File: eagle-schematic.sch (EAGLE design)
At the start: 30 parts, among them IC1 74HC595N, IC2 74HC595N, IC3 74HC595N, IC4 74HC595N, J1 DCJ0202, M1 DC-DC_5-15V_TO_5V

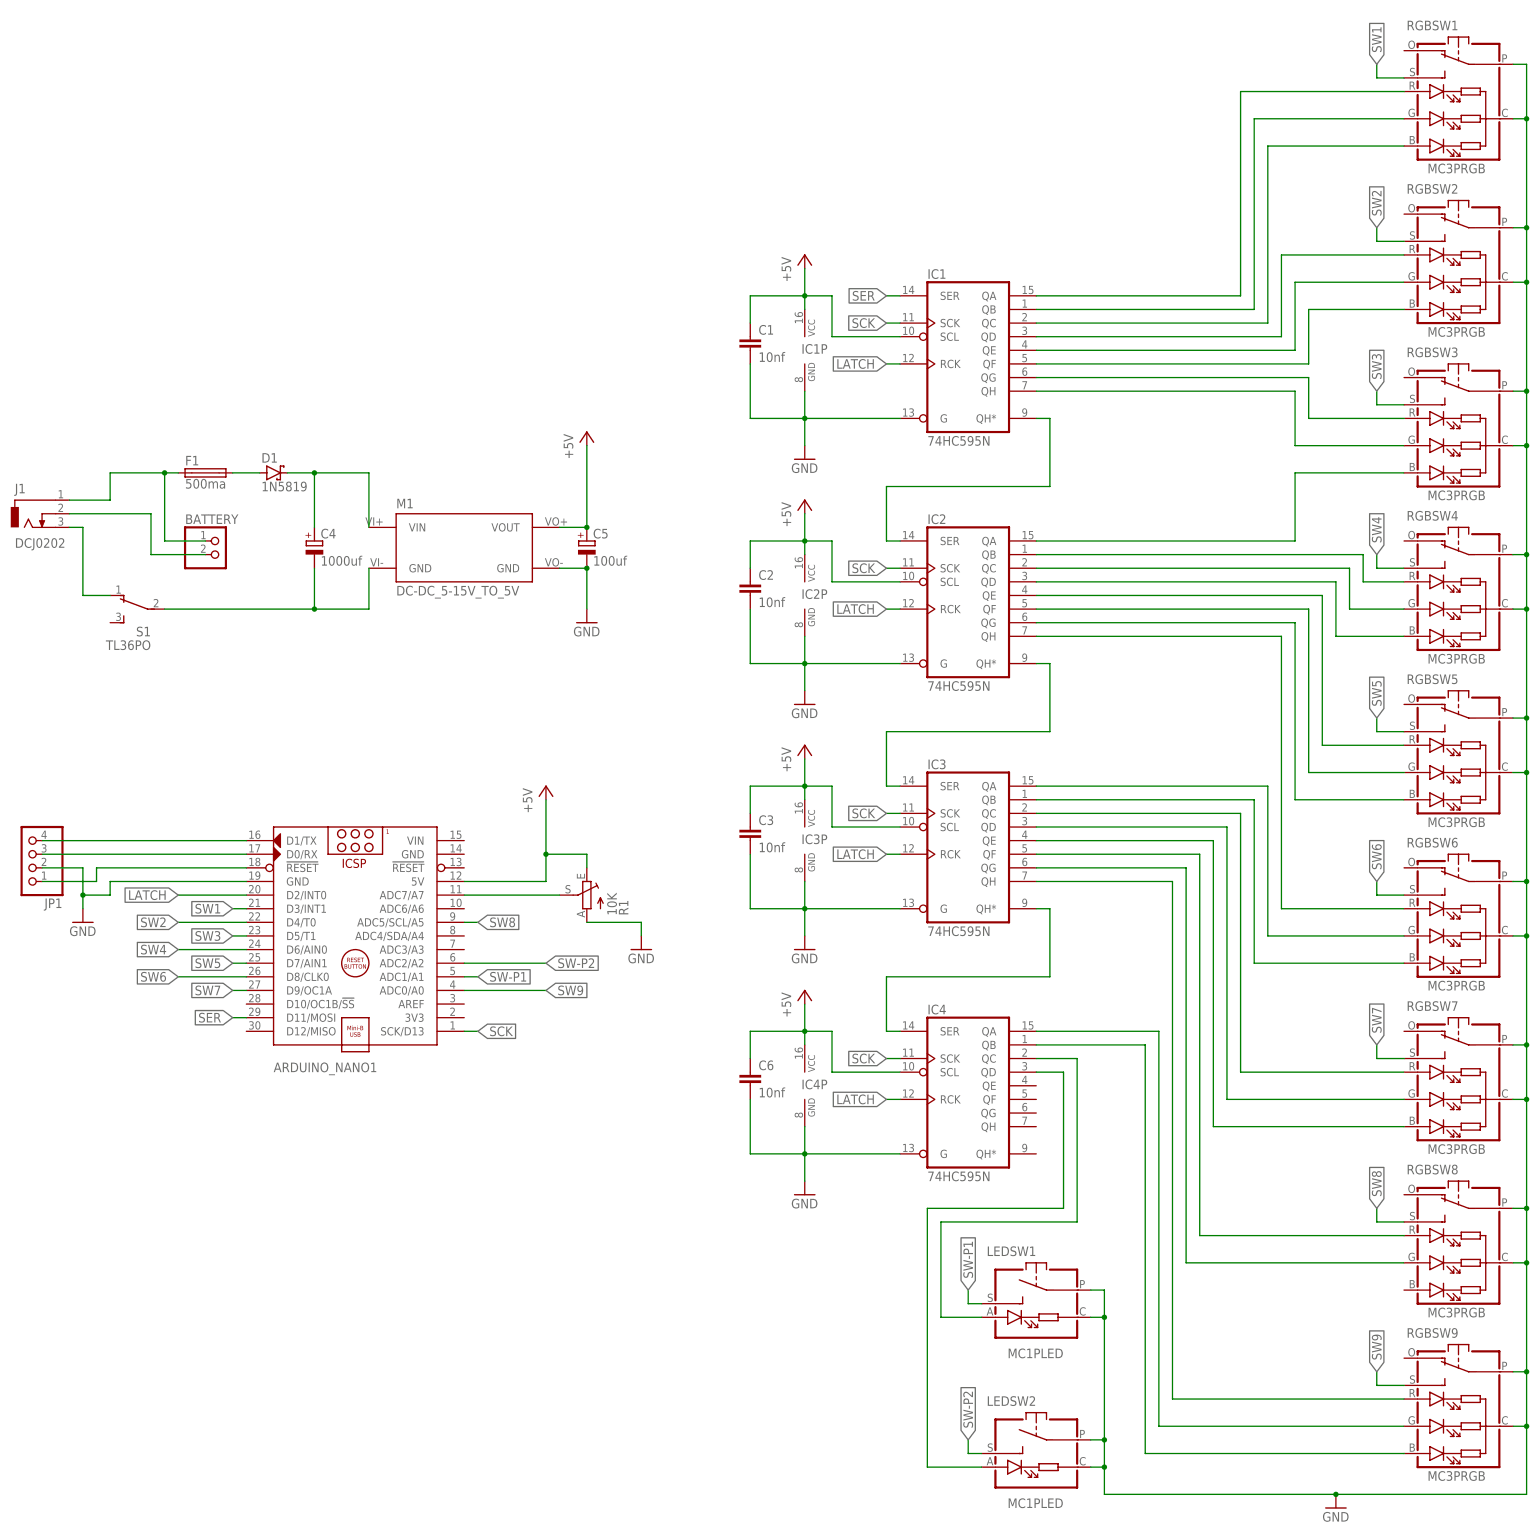
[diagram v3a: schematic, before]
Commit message: Updated libraries and part numbering
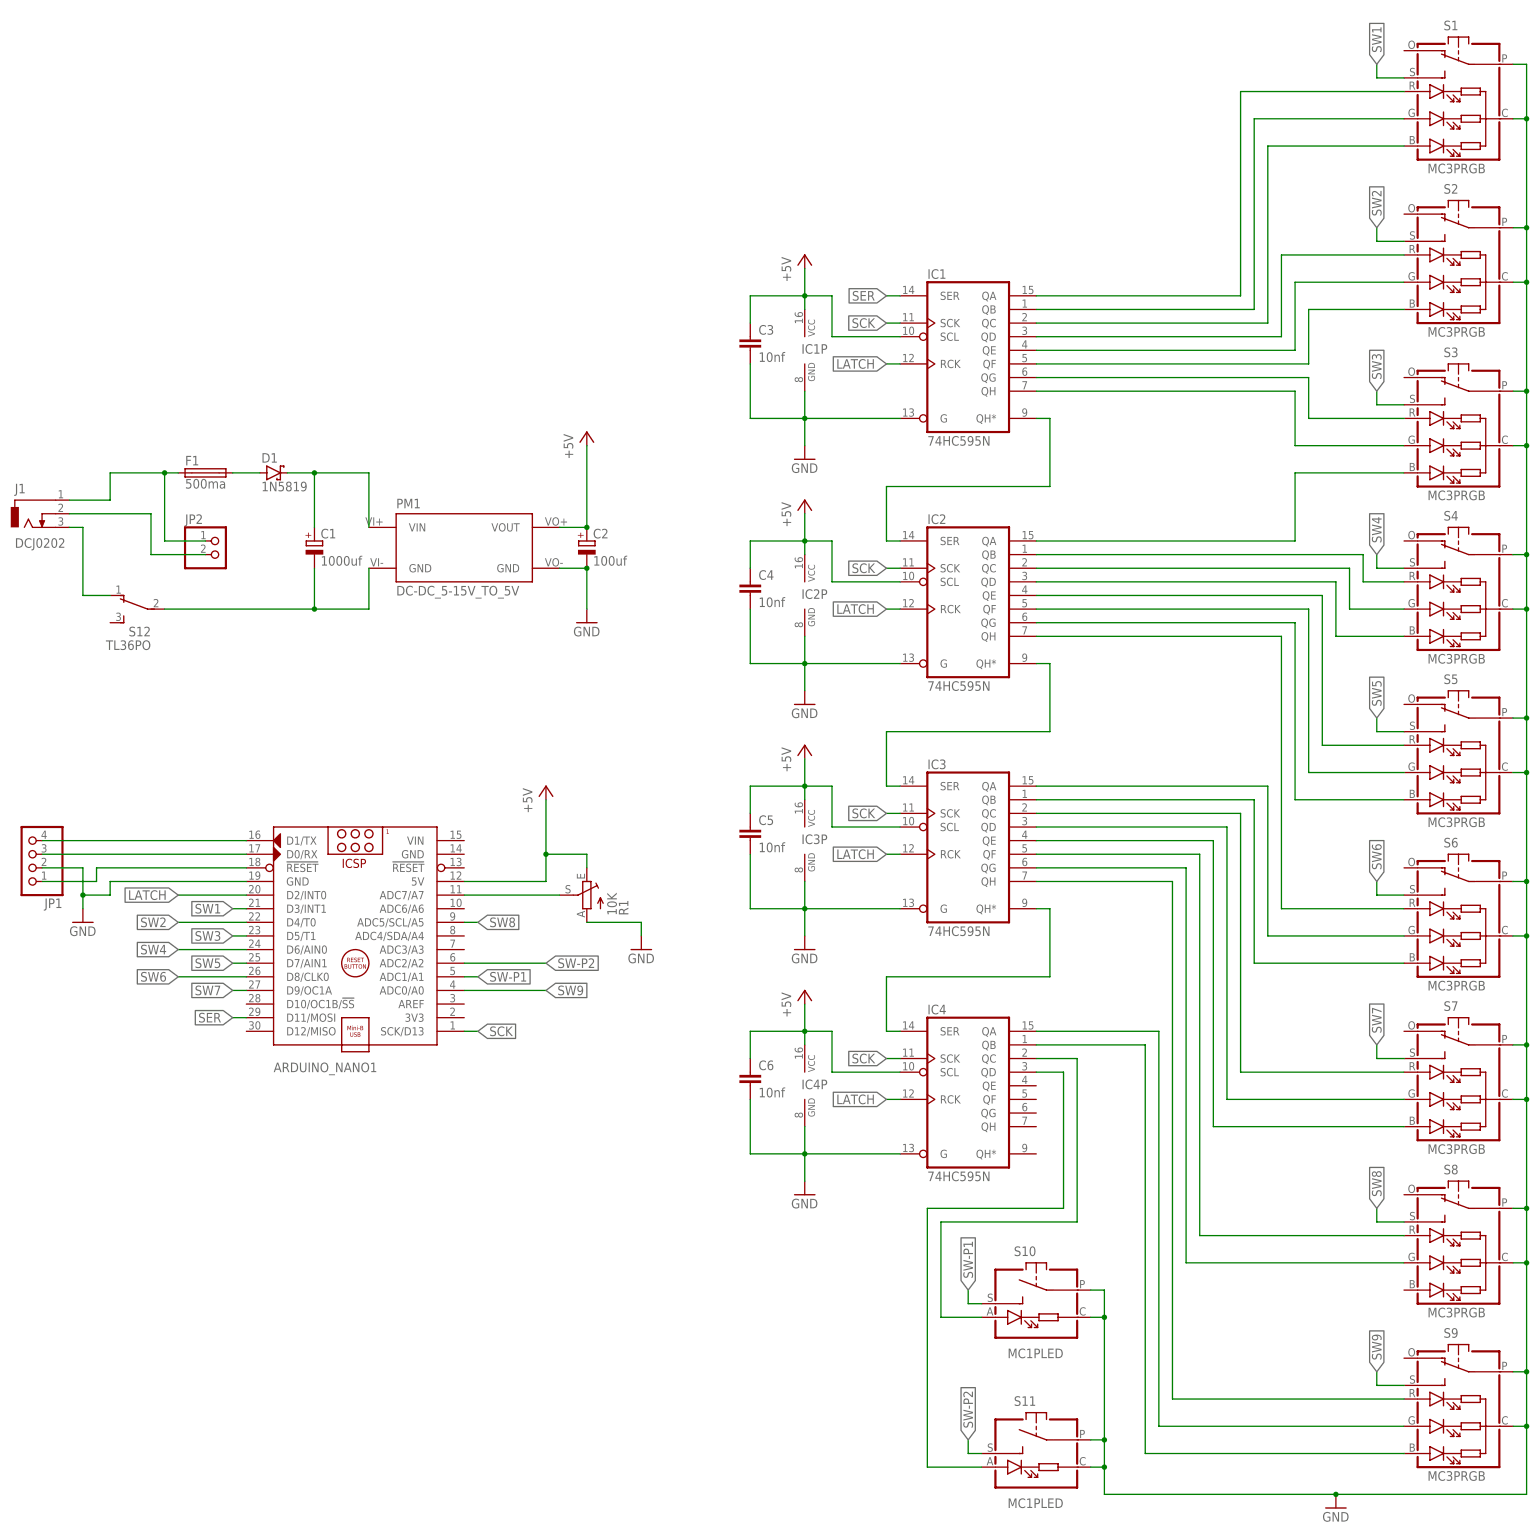
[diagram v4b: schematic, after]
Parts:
- removed RGBSW1: MC3PRGB, switches-custom:MC3PRGB
- added S12: TL36PO, switch:TL36PO
- C1: value 10nf -> 1000uf; device rcl:C-EU025-024X044 -> rcl:CPOL-EUE5-13
- C2: value 10nf -> 100uf; device rcl:C-EU025-024X044 -> rcl:CPOL-EUE2.5-5
- C4: value 1000uf -> 10nf; device rcl:CPOL-EUE5-13 -> rcl:C-EU025-024X044
- C5: value 100uf -> 10nf; device rcl:CPOL-EUE2.5-5 -> rcl:C-EU025-024X044
- S1: value TL36PO -> MC3PRGB; device switch:TL36PO -> switches-custom:MC3PRGB
- renumbered BATTERY to JP2, LEDSW1 to S10, LEDSW2 to S11, M1 to PM1, RGBSW2 to S2, RGBSW3 to S3, RGBSW4 to S4, RGBSW5 to S5, RGBSW6 to S6, RGBSW7 to S7, RGBSW8 to S8, RGBSW9 to S9
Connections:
- net +5V: now also C2.+, C4.1, C5.1; no longer C1.1, C2.1, C5.+
- net GND: now also C2.-, C4.2, C5.2, S1.C, S1.P; no longer C1.2, C2.2, C5.-, RGBSW1.C, RGBSW1.P
- net N$10: now also S1.R; no longer RGBSW1.R
- net N$11: now also S1.G; no longer RGBSW1.G
- net N$12: now also S1.B; no longer RGBSW1.B
- net N$6: now also S12.O; no longer S1.O
- net N$8: now also C1.+; no longer C4.+
- net N$9: now also C1.-, S12.P; no longer C4.-, S1.P
- net SW1: now also S1.S; no longer RGBSW1.S
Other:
- moved on the sheet: C3
